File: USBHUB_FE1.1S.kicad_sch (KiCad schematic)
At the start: 20 parts

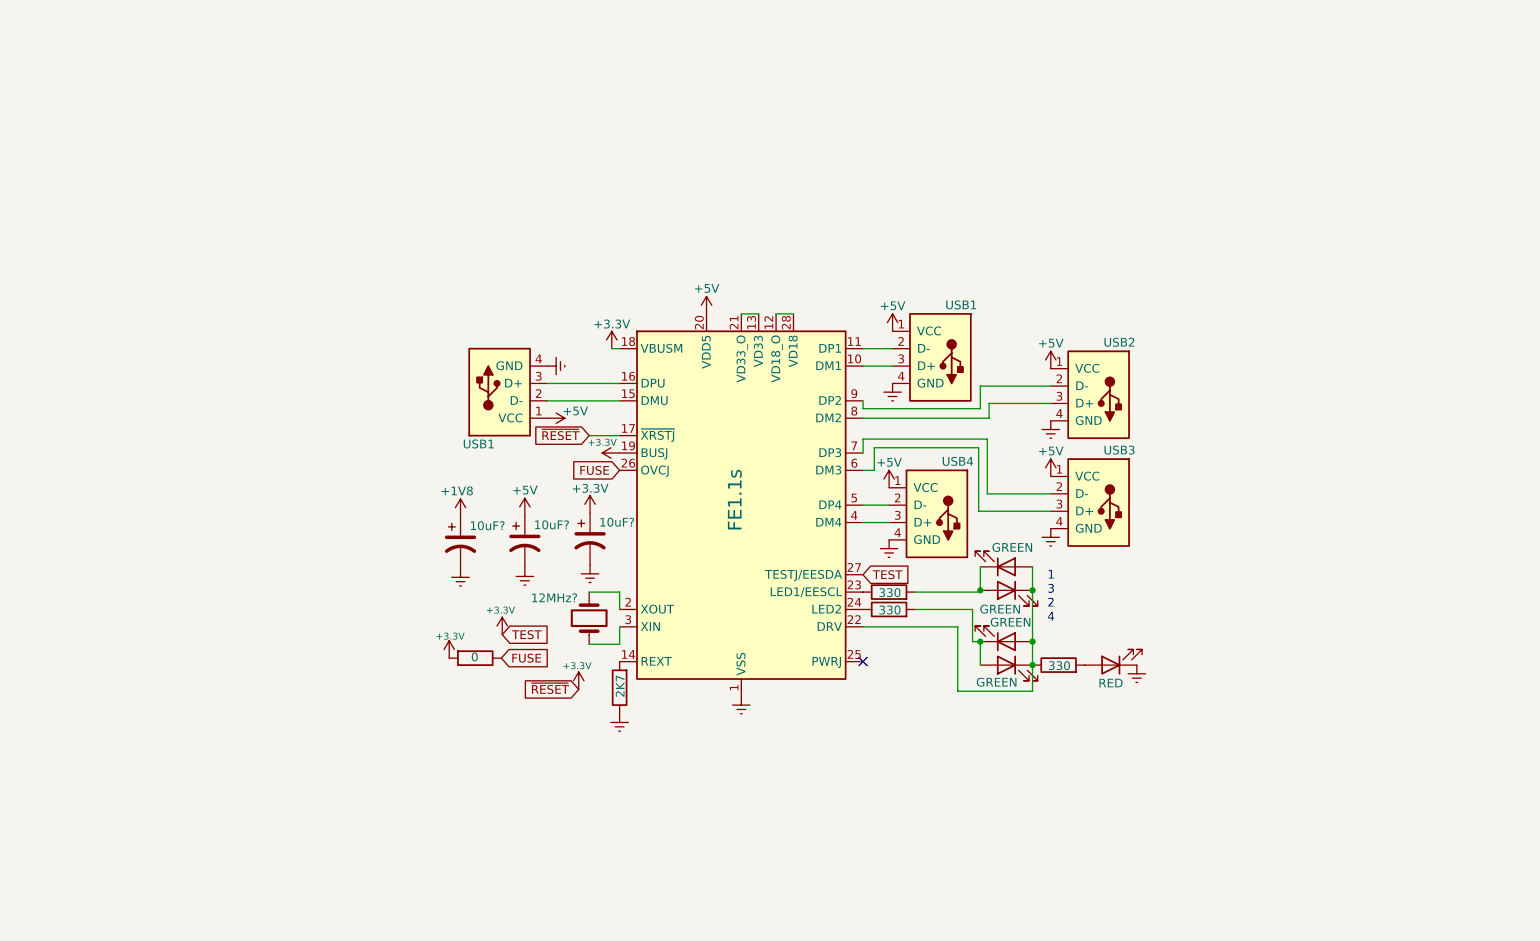
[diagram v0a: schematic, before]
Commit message: Adds capacitors and ferrite beads
Also a Fatrnell BOM.
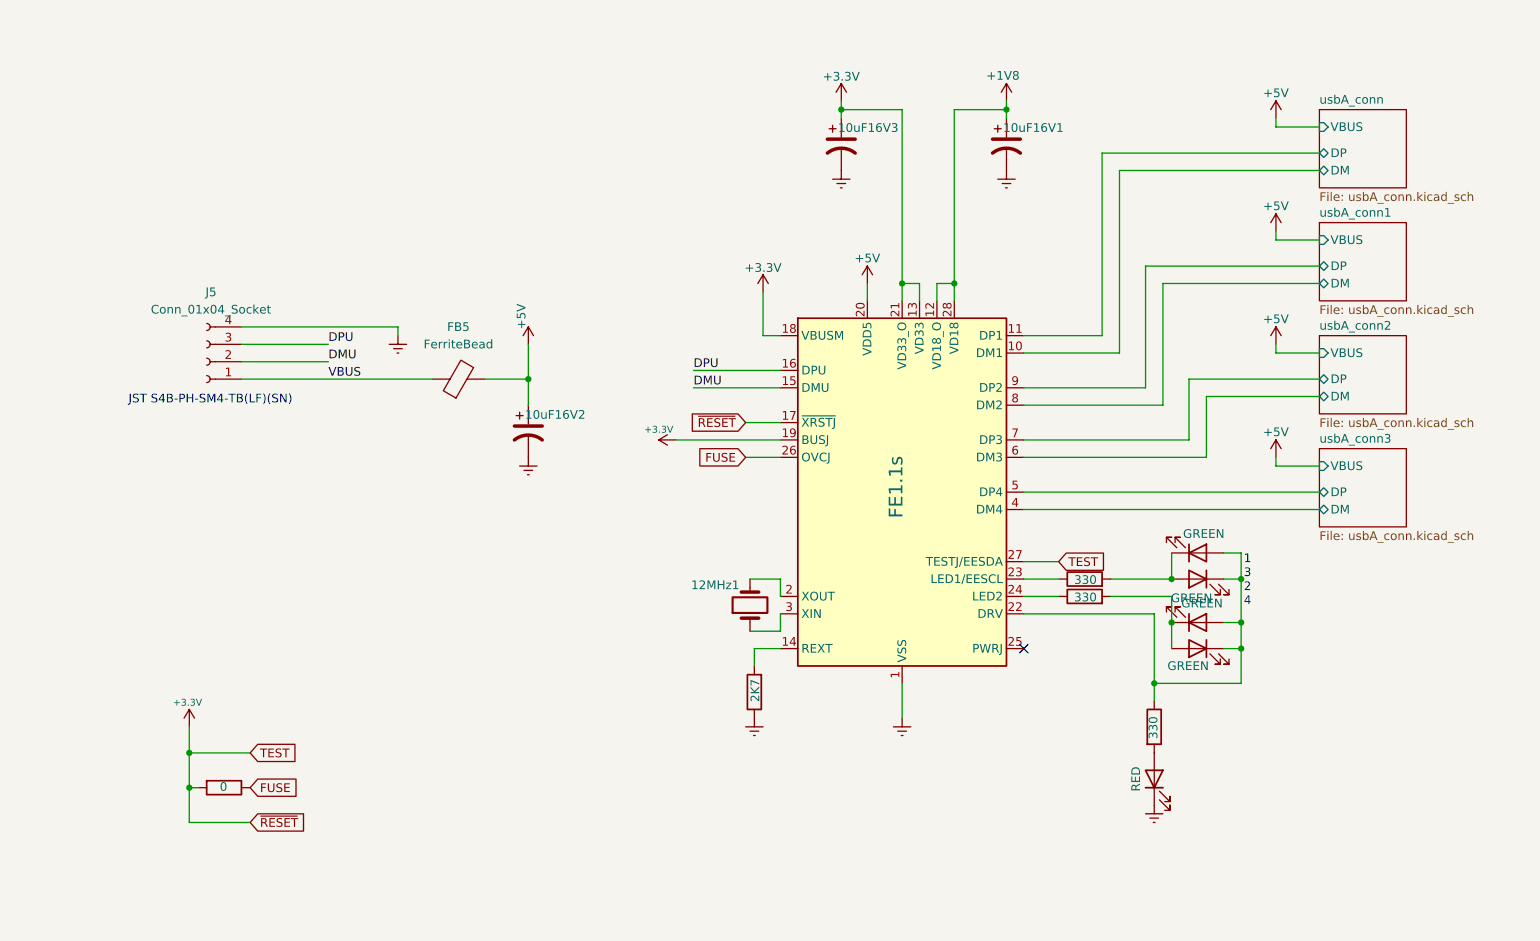
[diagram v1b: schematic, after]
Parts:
- removed 10uF? (x2): C_Polarized_US, symbol Device:C_Polarized_US
- removed D?: RED, symbol Device:LED
- removed J? (x2): USB1, symbol Connector:USB_A
- removed J?: USB4, symbol Connector:USB_A
- removed J?: USB2, symbol Connector:USB_A
- removed J?: USB3, symbol Connector:USB_A
- removed R?: 330, symbol Device:R
- added 10uF16V1, 10uF16V2: C_Polarized_US, Capacitor_SMD:C_0805_2012Metric, symbol Device:C_Polarized_US
- added D1: RED, LED_SMD:LED_0805_2012Metric, symbol Device:LED
- added FB5: FerriteBead, Inductor_SMD:L_0805_2012Metric, symbol Device:FerriteBead
- added J5: Conn_01x04_Socket, Connector_JST:JST_PH_S4B-PH-SM4-TB_1x04-1MP_P2.00mm_Horizontal, symbol Connector:Conn_01x04_Socket
- added R1: 330, Resistor_SMD:R_0805_2012Metric, symbol Device:R
- 10uF16V3: renamed from 10uF?; footprint (none) -> Capacitor_SMD:C_0805_2012Metric; FarnellRef (none) -> 3013485RL
- 12MHz1: renamed from 12MHz?; footprint (none) -> Crystal:Crystal_SMD_TXC_AX_8045-2Pin_8.0x4.5mm; FarnellRef (none) -> 2419395
- D2, D3, D4, D5: renamed from D?; footprint (none) -> LED_SMD:LED_0805_2012Metric
- R2, R3, R4, R5: renamed from R?; footprint (none) -> Resistor_SMD:R_0805_2012Metric
- gave numbers to parts that had none: 1
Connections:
- net +1V8: now also U1.12 (VD18_O), U1.28 (VD18), 10uF16V1.1
- net +3V3: now also U1.13 (VD33), U1.21 (VD33_O)
- net +5V: now also 10uF16V2.1, FB5.2
- net Earth: now also 10uF16V1.2, 10uF16V2.2, D1.1 (K), J5.4 (Pin_4)
- net at D2.2 (A), D3.1 (K), D4.2 (A)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: now also R1.1
- net usbA_conn/DP: now reaches U1.11 (DP1)
- net usbA_conn/DM: now reaches U1.10 (DM1)
- net DMU: now reaches U1.15 (DMU)
- net DMU: now also J5.2 (Pin_2)
- net DPU: now reaches U1.16 (DPU)
- net DPU: now also J5.3 (Pin_3)
- net usbA_conn3/DP: now reaches U1.5 (DP4)
- net usbA_conn3/DM: now reaches U1.4 (DM4)
- net usbA_conn1/DP: now reaches U1.9 (DP2)
- net usbA_conn1/DM: now reaches U1.8 (DM2)
- net usbA_conn2/DM: now reaches U1.6 (DM3)
- net usbA_conn2/DP: now reaches U1.7 (DP3)
- new net: D1.2 (A), R1.2
- new net VBUS: FB5.1, J5.1 (Pin_1)
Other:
- added sheet usbA_conn (usbA_conn.kicad_sch)
- added sheet usbA_conn1 (usbA_conn.kicad_sch)
- added sheet usbA_conn2 (usbA_conn.kicad_sch)
- added sheet usbA_conn3 (usbA_conn.kicad_sch)
- note added: "JST S4B-PH-SM4-TB(LF)(SN)"
- moved on the sheet: 10uF16V3, 12MHz1

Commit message: Finished schematic
The USB-A connector foortprint, 3D model, and symbol comes from Snap
EDA.
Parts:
- removed R2: 0, Resistor_SMD:R_0805_2012Metric, symbol Device:R
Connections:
- net FUSE: no longer names the net of U1.26 (OVCJ)
- no-connect marks 1 -> 2
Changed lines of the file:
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@@
   (junction (at 166.37 30.48) (diameter 0) (color 0 0 0 0)
   )
-  (junction (at 46.99 129.54) (diameter 0) (color 0 0 0 0)
-  )
   (junction (at 187.96 114.3) (diameter 0) (color 0 0 0 0)
   )
+  (no_connect (at 133.35 81.28))
   (no_connect (at 168.91 109.22))
   (wire (pts (xy 198.12 99.06) (xy 200.66 99.06))
@@
     (stroke (width 0) (type default))
   )
-  (wire (pts (xy 46.99 129.54) (xy 48.26 129.54))
-    (stroke (width 0) (type default))
-  )
   (wire (pts (xy 168.91 86.36) (xy 212.09 86.36))
     (stroke (width 0) (type default))
@@
     (stroke (width 0) (type default))
   )
-  (wire (pts (xy 46.99 129.54) (xy 46.99 124.46))
-    (stroke (width 0) (type default))
-  )
   (wire (pts (xy 181.61 99.06) (xy 190.5 99.06))
     (stroke (width 0) (type default))
@@
     (stroke (width 0) (type default))
   )
-  (wire (pts (xy 46.99 134.62) (xy 46.99 129.54))
+  (wire (pts (xy 46.99 124.46) (xy 46.99 134.62))
     (stroke (width 0) (type default))
   )
@@
   )
   (wire (pts (xy 153.67 55.88) (xy 153.67 58.42))
-    (stroke (width 0) (type default))
-  )
-  (wire (pts (xy 128.27 81.28) (xy 133.35 81.28))
     (stroke (width 0) (type default))
   )
@@
     )
   )
-  (global_label "FUSE" (shape input) (at 128.27 81.28 180) (fields_autoplaced)
-    (effects (font (size 1.27 1.27)) (justify right))
-    (property "Intersheetrefs" "${INTERSHEET_REFS}" (at 121.0793 81.3594 0)
-      (effects (font (size 1.27 1.27)) (justify right) hide)
-    )
-  )
   (global_label "~{RESET}" (shape input) (at 128.27 76.2 180) (fields_autoplaced)
     (effects (font (size 1.27 1.27)) (justify right))
@@
     )
   )
-  (global_label "FUSE" (shape input) (at 55.88 129.54 0) (fields_autoplaced)
-    (effects (font (size 1.27 1.27)) (justify left))
-    (property "Intersheetrefs" "${INTERSHEET_REFS}" (at 63.0707 129.4606 0)
-      (effects (font (size 1.27 1.27)) (justify left) hide)
-    )
-  )
   (symbol (lib_id "Device:FerriteBead") (at 86.36 69.85 90) (unit 1)
     (in_bom yes) (on_board yes) (dnp no) (fields_autoplaced)
@@
         )
       )
-    )
-  )
-  (symbol (lib_id "Device:R") (at 52.07 129.54 270) (unit 1)
-    (in_bom yes) (on_board yes) (dnp no)
-    (property "Reference" "R2" (at 53.3401 131.445 0)
-      (effects (font (size 1.27 1.27)) (justify left) hide)
-    )
-    (property "Value" "0" (at 51.435 129.413 90)
-      (effects (font (size 1.27 1.27)) (justify left))
-    )
-    (property "Footprint" "Resistor_SMD:R_0805_2012Metric" (at 52.07 127.762 90)
-      (effects (font (size 1.27 1.27)) hide)
-    )
-    (property "Datasheet" "~" (at 52.07 129.54 0)
-      (effects (font (size 1.27 1.27)) hide)
-    )
-    (pin "1")
-    (pin "2")
-    (instances
-      (project "USBHUB_FE1.1S"
-        (path "/fe375ede-0629-4c66-9d75-419b70ed1e04"
-          (reference "R2") (unit 1)
-        )
-      )

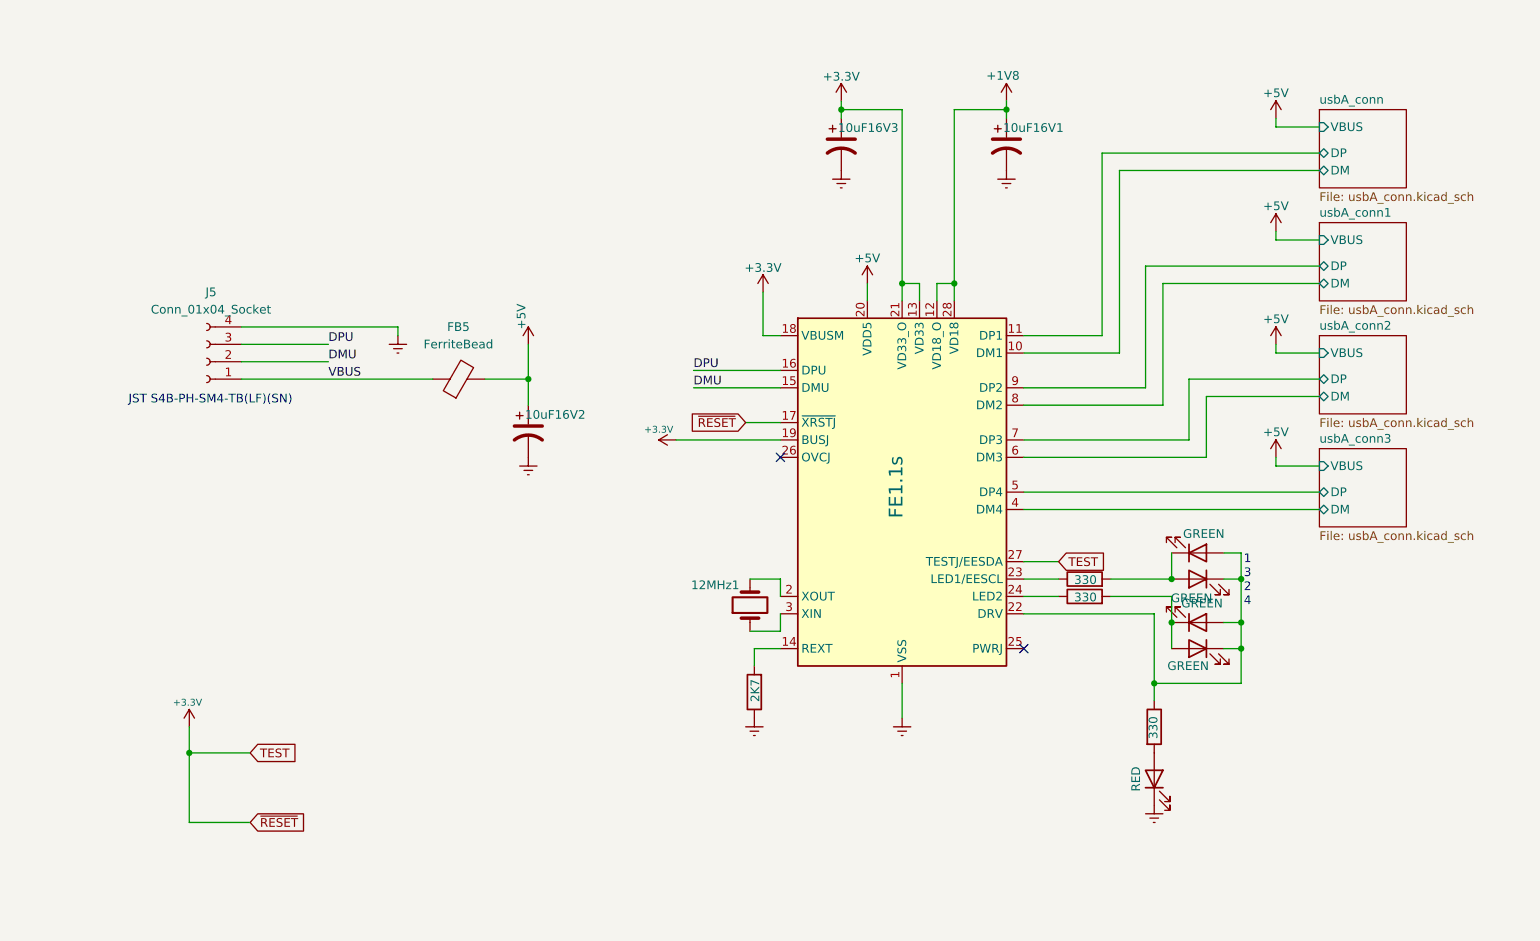
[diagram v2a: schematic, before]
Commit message: ERC pass but one ground pin on th eUSB-A connector.
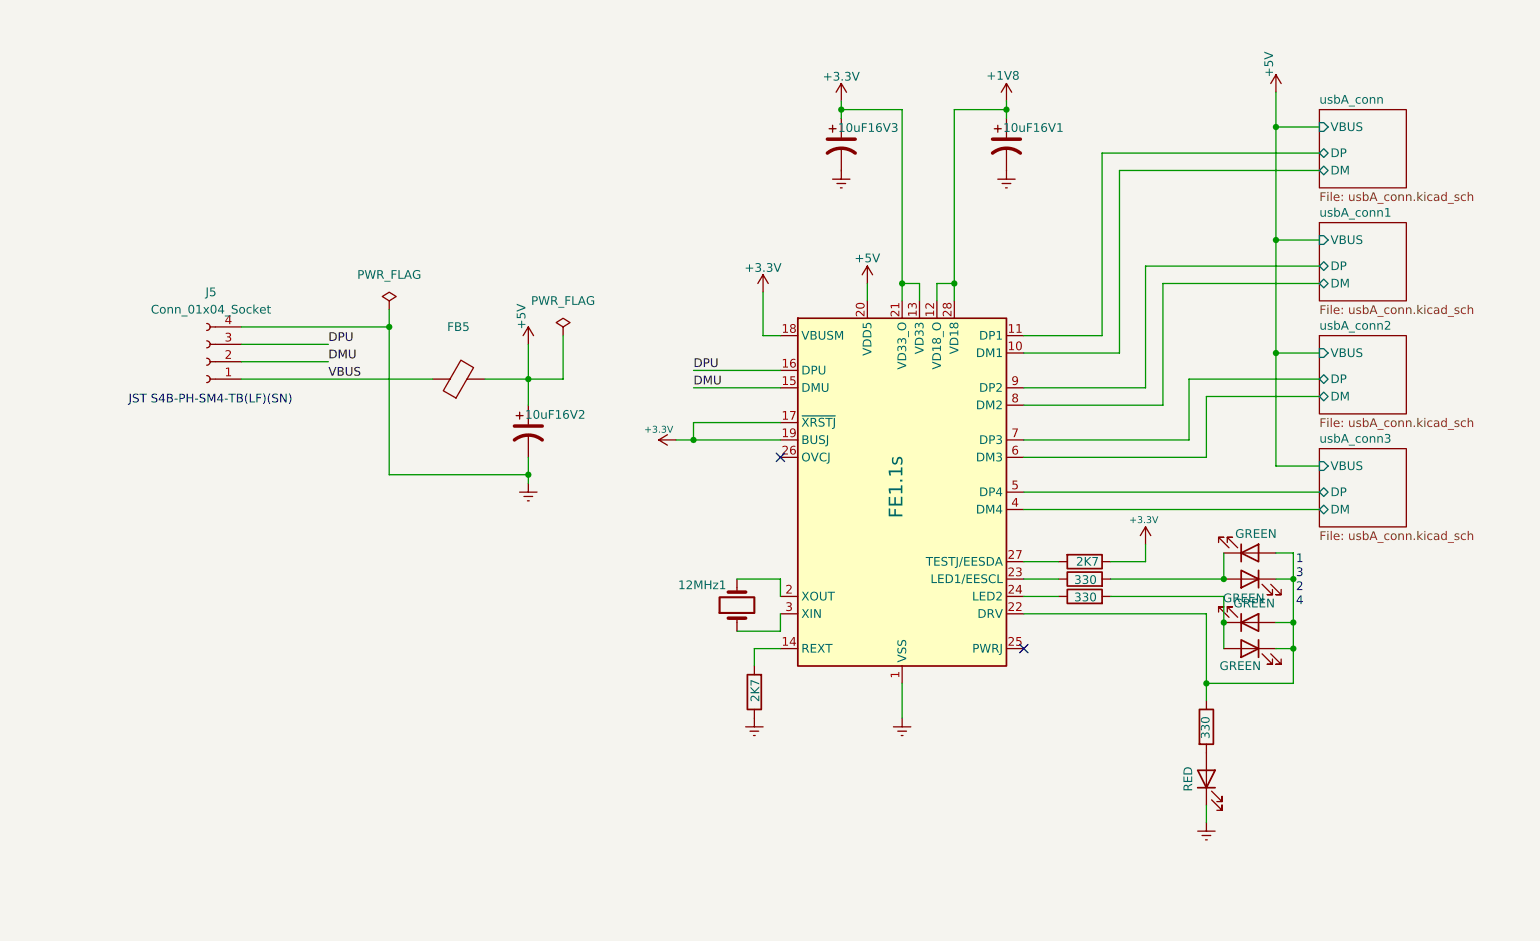
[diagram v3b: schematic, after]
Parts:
- added R2: 2K7, Resistor_SMD:R_0805_2012Metric, symbol Device:R
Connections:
- net +3V3 renamed +3.3V
- net +3.3V: now also R2.1; no longer U1.27 (TESTJ/EESDA)
- new net: R2.2, U1.27 (TESTJ/EESDA)
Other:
- moved on the sheet: 12MHz1

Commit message: Routed, Rev1
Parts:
- removed 10uF16V1, 10uF16V2, 10uF16V3: C_Polarized_US, Capacitor_SMD:C_0805_2012Metric, symbol Device:C_Polarized_US
- removed 12MHz1: Crystal, Crystal:Crystal_SMD_TXC_AX_8045-2Pin_8.0x4.5mm, symbol Device:Crystal
- added C5, C6, C7: 10uF16V, Capacitor_SMD:C_0805_2012Metric, symbol Device:C
- added FID1, FID2, FID3: Fiducial, Fiducial:Fiducial_0.5mm_Mask1.5mm, symbol Mechanical:Fiducial
- added H1, H2, H3, H4, H5: MountingHole_Pad, MountingHole:MountingHole_3.2mm_M3_DIN965_Pad_TopBottom, symbol Mechanical:MountingHole_Pad
- added Y1: Crystal_GND24, Crystal:Crystal_SMD_3225-4Pin_3.2x2.5mm, symbol Device:Crystal_GND24
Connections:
- net +1V8: now also C5.1
- net +3.3V: now also C6.1
- net +5V: now also C7.1
- net at U1.3 (XIN): now also Y1.1
- net at U1.2 (XOUT): now also Y1.3
- net DMU renamed DU-
- net DPU renamed DU+
- net Earth renamed GND
- net GND: now also C5.2, C6.2, C7.2, H1.1, H2.1, H3.1, H4.1, H5.1, Y1.2, Y1.4
- net usbA_conn/DM renamed D1-
- net usbA_conn/DP renamed D1+
- net usbA_conn1/DM renamed D2-
- net usbA_conn1/DP renamed D2+
- net usbA_conn2/DM renamed D3-
- net usbA_conn2/DP renamed D3+
- net usbA_conn3/DM renamed D4-
- net usbA_conn3/DP renamed D4+
